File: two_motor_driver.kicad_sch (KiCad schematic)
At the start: 24 parts, among them J1 Conn_01x02, J2 Conn_01x02, J3 Conn_01x08, M1 Conn_01x03, M2 Conn_01x03, SW1 SW_SPDT, SW2 SW_Push, U5 my_buck_boost

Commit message: pcb layout
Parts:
- removed M1, M2, TP2: Conn_01x03, Connector_PinHeader_2.54mm:PinHeader_1x03_P2.54mm_Vertical, symbol Connector_Generic:Conn_01x03
- added FOC1, FOC2: Conn_01x05, Connector_PinSocket_2.54mm:PinSocket_1x05_P2.54mm_Vertical, symbol Connector_Generic:Conn_01x05
- added POT1, RC1, RC2, RC3, SEL1, SEL2: Conn_01x03, Connector_PinHeader_2.54mm:PinHeader_1x03_P2.54mm_Vertical, symbol Connector_Generic:Conn_01x03
- J3: footprint (none) -> Connector_PinSocket_2.54mm:PinSocket_1x08_P2.54mm_Vertical
- renumbered C16 to C1, C15 to C2, D4 to D1, J2 to SEL3
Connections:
- net +3.3V: now also POT1.1 (Pin_1); no longer U5.7 (Reg_out), U5.8 (Reg_out)
- net FOC1_EN: now also FOC1.1 (Pin_1)
- net FOC1_PWM_A: now also FOC1.4 (Pin_4)
- net FOC1_PWM_B: now also FOC1.3 (Pin_3)
- net FOC1_PWM_C: now also FOC1.2 (Pin_2)
- net FOC2_EN: now also FOC2.1 (Pin_1)
- net FOC2_PWM_A: now also FOC2.4 (Pin_4)
- net FOC2_PWM_B: now also FOC2.3 (Pin_3)
- net FOC2_PWM_C: now also FOC2.2 (Pin_2)
- net GND: now also FOC1.5 (Pin_5), FOC2.5 (Pin_5), POT1.3 (Pin_3), RC1.3 (Pin_3), RC2.3 (Pin_3), RC3.3 (Pin_3)
- net MPU6050_SDA: now also SEL2.3 (Pin_3); no longer A1.23 (SDA/A4)
- net RC_Mode: now also RC3.1 (Pin_1)
- net RC_Throttle: now also RC1.1 (Pin_1)
- net +5V: now reaches A1.27 (VUSB/5V)
- net +5V: now also U5.7 (Reg_out), U5.8 (Reg_out), RC1.2 (Pin_2), RC2.2 (Pin_2), RC3.2 (Pin_2)
- net Vcc_Sense: no longer names the net of 10k_2.1, 90k_2.2, D1.3
- net Vcc_Sense: now also SEL1.3 (Pin_3); no longer A1.26 (A7)
- new net A4_in: A1.23 (SDA/A4), SEL2.2 (Pin_2)
- new net A7_in: A1.26 (A7), SEL1.2 (Pin_2)
- new net POT: POT1.2 (Pin_2), SEL2.1 (Pin_1)
- new net RC_Steering: RC2.1 (Pin_1), SEL1.1 (Pin_1)
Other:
- note added: "Pin Signal ---|--------- D1 | TP_ESP32 D2 | FOC1_EN D3 | FOC1_PWM_A D4 | FOC1_PWM_B D5 | FOC1_PWM_C D6 | FOC2_EN D7 | FOC2_PWM_A D8 | FOC2_PWM_B D9 | FOC2_PWM_C D10| ENC1_A D11| ENC1_B D12| ENC2_A D13| On board LED A2 | ENC2_B A4 | MPU6050_SDA / POT A5 | MPU6050_SCL A0 | RC_Throttle A1 | RC_Mode A3 | Hall_1 A6 | Hall_2 A7 | RC_Steering / Vcc IN"
- note added: "Select RC or Vcc in"
- note added: "Select potentiometer or MPU6050_SDA"
- note removed: "Pin Signal ---|--------- D1 | TP_ESP32 D2 | FOC1_EN D3 | FOC1_PWM_A D4 | FOC1_PWM_B D5 | FOC1_PWM_C D6 | FOC2_EN D7 | FOC2_PWM_A D8 | FOC2_PWM_B D9 | FOC2_PWM_C D10| ENC1_A D11| ENC1_B D12| ENC2_A D13| On board LED A2 | ENC2_B A4 | MPU6050_SDA A5 | MPU6050_SCL A0 | RC_Throttle A1 | RC_Mode A3 | Hall_1 A6 | Hall_2 A7 | Vcc_Sense"
- moved on the sheet: 10k_2, 4.7nF_1, 4.7nF_2, 90k_2, A1, C1, C2, D1, J3, R1, R2, TP1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

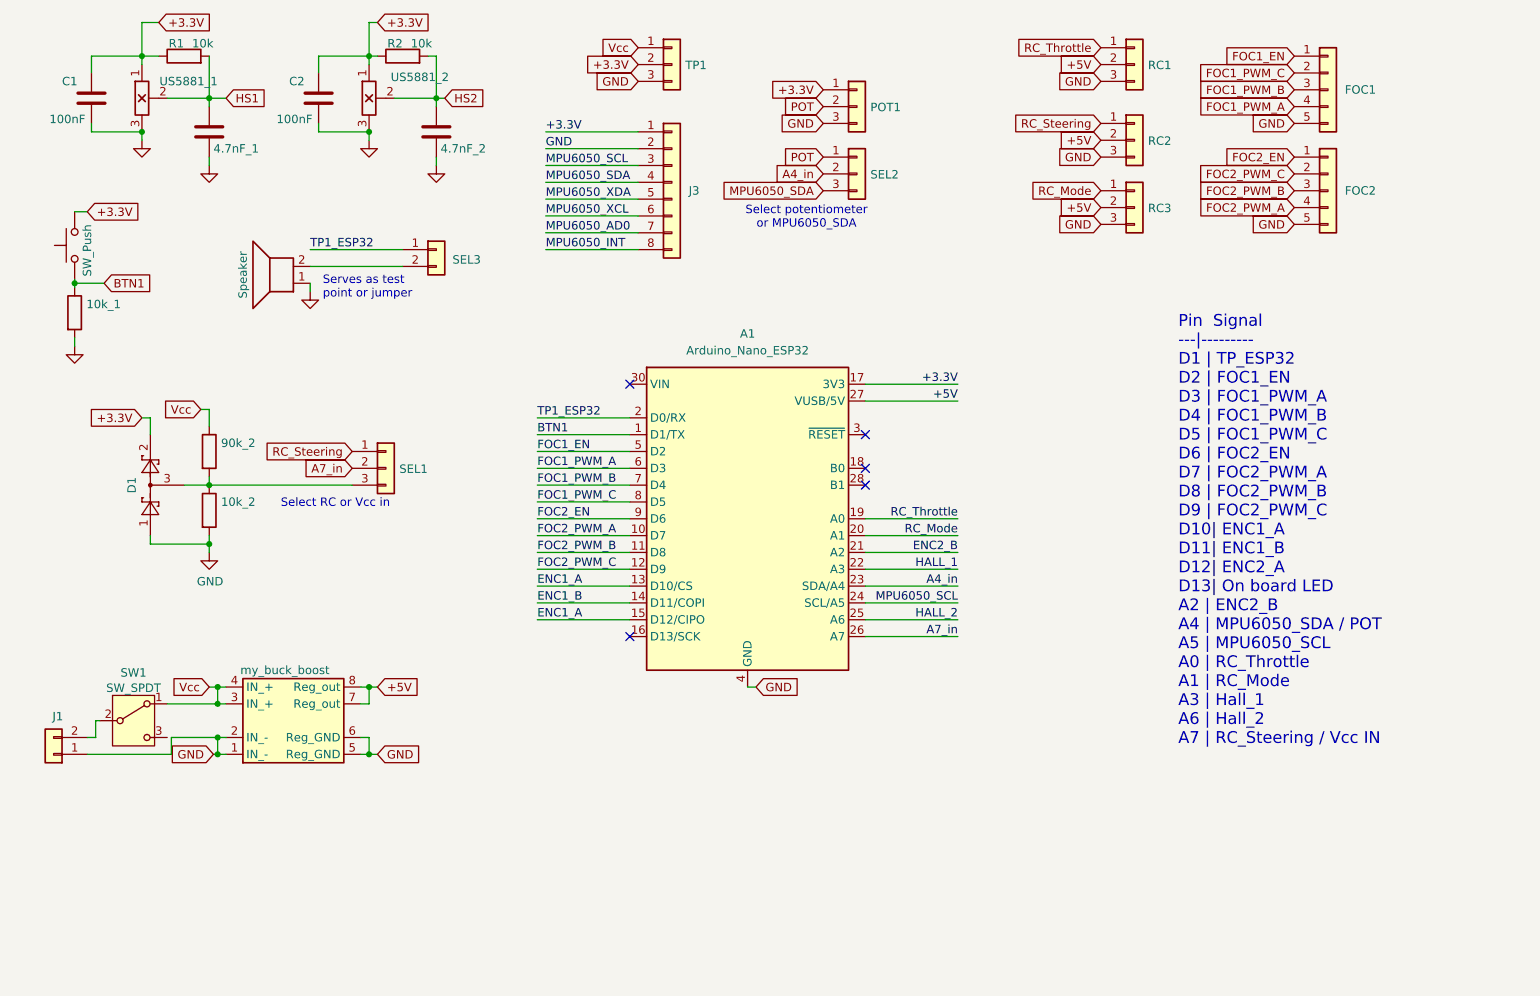
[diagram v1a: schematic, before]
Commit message: converted to teensy 4.0
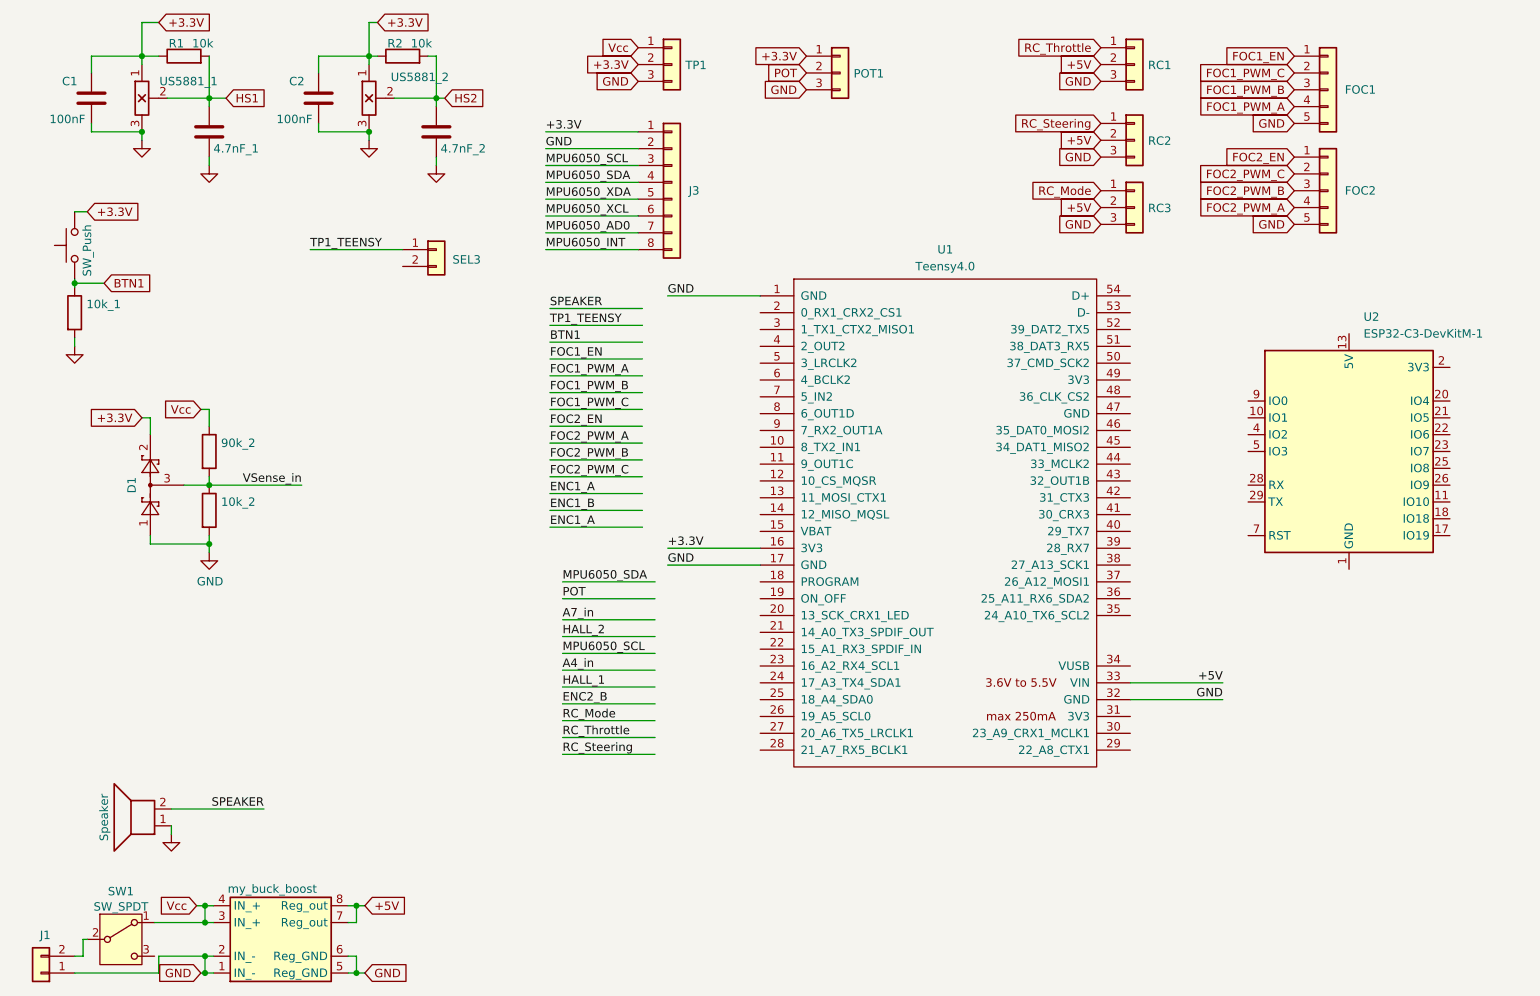
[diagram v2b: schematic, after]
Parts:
- removed A1: Arduino_Nano_ESP32, Module:Arduino_Nano, symbol MCU_Module:Arduino_Nano_ESP32
- removed SEL1, SEL2: Conn_01x03, Connector_PinHeader_2.54mm:PinHeader_1x03_P2.54mm_Vertical, symbol Connector_Generic:Conn_01x03
- added U1: Teensy4.0, simpleFOC_board:Teensy40, symbol teensy:Teensy4.0
- added U2: ESP32-C3-DevKitM-1, RF_Module:ESP32-C3-DevKitM-1, symbol RF_Module:ESP32-C3-DevKitM-1
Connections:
- net +3.3V: now also U1.16 (3V3)
- net +5V: now also U1.33 (VIN)
- net GND: now also U1.1 (GND), U1.17 (GND), U1.32 (GND)
- net VSense_in: now reaches 10k_2.1, 90k_2.2, D1.3
- net at SEL3.2 (Pin_2): no longer LS1.2
- net TP1_ESP32 renamed TP1_TEENSY
- new net: U2.1 (GND), U2.12 (GND), U2.15 (GND), U2.16 (GND), U2.19 (GND), U2.24 (GND), U2.27 (GND), U2.30 (GND), U2.6 (GND), U2.8 (GND)
- new net: U2.13 (5V), U2.14 (5V)
- new net: U2.2 (3V3), U2.3 (3V3)
- new net SPEAKER: LS1.2
- no-connect marks 5 -> 0
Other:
- note removed: "Pin Signal ---|--------- D1 | TP_ESP32 D2 | FOC1_EN D3 | FOC1_PWM_A D4 | FOC1_PWM_B D5 | FOC1_PWM_C D6 | FOC2_EN D7 | FOC2_PWM_A D8 | FOC2_PWM_B D9 | FOC2_PWM_C D10| ENC1_A D11| ENC1_B D12| ENC2_A D13| On board LED A2 | ENC2_B A4 | MPU6050_SDA / POT A5 | MPU6050_SCL A0 | RC_Throttle A1 | RC_Mode A3 | Hall_1 A6 | Hall_2 A7 | RC_Steering / Vcc IN"
- note removed: "Select RC or Vcc in"
- note removed: "Select potentiometer or MPU6050_SDA"
- note removed: "Serves as test point or jumper"
- moved on the sheet: J1, POT1, SW1

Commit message: started layout
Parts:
- removed POT1, TP1: Conn_01x03, Connector_PinHeader_2.54mm:PinHeader_1x03_P2.54mm_Vertical, symbol Connector_Generic:Conn_01x03
- removed SEL3: Conn_01x02, Connector_PinHeader_2.54mm:PinHeader_1x02_P2.54mm_Vertical, symbol Connector_Generic:Conn_01x02
- added ENC1, ENC2: J1, Connector_PinSocket_2.54mm:PinSocket_1x04_P2.54mm_Vertical, symbol Connector_Generic:Conn_01x04
- added J2: ESP PROG, Connector_PinSocket_2.54mm:PinSocket_1x04_P2.54mm_Vertical, symbol Connector_Generic:Conn_01x04
- added J5, J6, J7: Conn_01x01, Connector_PinSocket_2.54mm:PinSocket_1x01_P2.54mm_Vertical, symbol Connector_Generic:Conn_01x01
- added M1, M2: Conn_01x02, Connector_PinHeader_2.54mm:PinHeader_1x02_P2.54mm_Vertical, symbol Connector_Generic:Conn_01x02
- LS1: footprint (none) -> CDS-13138-SMT-TR:SPKR_CDS-13138-SMT-TR
- SW2: footprint (none) -> Button_Switch_SMD:SW_Push_SPST_NO_Alps_SKRK
- renumbered 10k_2 to 10k_1, 10k_1 to 10k_2, R1 to 10k_3, R2 to 10k_4, 90k_2 to 90k_1
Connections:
- net HS1 is gone; now on net HALL_1: 10k_3.2, 4.7nF_1.1, US5881_1.2 (out)
- net HS2 is gone; now on net HALL_2: 10k_4.2, 4.7nF_2.1, US5881_2.2 (out)
- net +3.3V: now also U2.2 (3V3), U2.3 (3V3), ENC1.1 (Pin_1), ENC2.1 (Pin_1), J2.1 (Pin_1), J6.1 (Pin_1)
- net +5V: now also J5.1 (Pin_1)
- net BTN1: now also U1.29 (22_A8_CTX1)
- net ENC1_A: now also U1.2 (0_RX1_CRX2_CS1), ENC1.2 (Pin_2)
- net ENC1_B: now also U1.3 (1_TX1_CTX2_MISO1), ENC1.3 (Pin_3)
- net ENC2_B: now also U1.22 (15_A1_RX3_SPDIF_IN), ENC2.3 (Pin_3)
- net FOC1_EN: now also U1.4 (2_OUT2)
- net FOC1_PWM_A: now also U1.7 (5_IN2)
- net FOC1_PWM_B: now also U1.6 (4_BCLK2)
- net FOC1_PWM_C: now also U1.5 (3_LRCLK2)
- net FOC2_EN: now also U1.8 (6_OUT1D)
- net FOC2_PWM_A: now also U1.11 (9_OUT1C)
- net FOC2_PWM_B: now also U1.10 (8_TX2_IN1)
- net FOC2_PWM_C: now also U1.9 (7_RX2_OUT1A)
- net GND: now also LS1.2, U2.1 (GND), U2.12 (GND), U2.15 (GND), U2.16 (GND), U2.19 (GND), U2.24 (GND), U2.27 (GND), U2.30 (GND), U2.6 (GND), U2.8 (GND), ENC1.4 (Pin_4), ENC2.4 (Pin_4), J2.4 (Pin_4), J7.1 (Pin_1), M1.2 (Pin_2), M2.2 (Pin_2); no longer LS1.1
- net HALL_1: now also U2.21 (IO5)
- net HALL_2: now also U2.20 (IO4)
- net MPU6050_SCL: now also U1.26 (19_A5_SCL0)
- net MPU6050_SDA: now also U1.25 (18_A4_SDA0)
- net RC_Mode: now also U1.24 (17_A3_TX4_SDA1)
- net RC_Steering: now also U1.28 (21_A7_RX5_BCLK1)
- net RC_Throttle: now also U1.27 (20_A6_TX5_LRCLK1)
- net SPEAKER: now also LS1.1, U1.30 (23_A9_CRX1_MCLK1); no longer LS1.2
- net VSense_in: now also U1.21 (14_A0_TX3_SPDIF_OUT)
- net Vcc: now also M1.1 (Pin_1), M2.1 (Pin_1)
- net ESP32_CS: now reaches U2.11 (IO10)
- net ESP32_CS: now also U1.12 (10_CS_MQSR)
- net ESP32_CLK: now reaches U2.22 (IO6)
- net ESP32_CLK: now also U1.20 (13_SCK_CRX1_LED)
- net ESP32_MOSI: now reaches U2.23 (IO7)
- net ESP32_MOSI: now also U1.13 (11_MOSI_CTX1)
- net ESP32_RX: now reaches U2.28 (RX)
- net ESP32_RX: now also J2.2 (Pin_2)
- net ESP32_TX: now reaches U2.29 (TX)
- net ESP32_TX: now also J2.3 (Pin_3)
- net ESP32_MISO: now reaches U2.4 (IO2)
- net ESP32_MISO: now also U1.14 (12_MISO_MQSL)
- net ENC2_A: now reaches U1.23 (16_A2_RX4_SCL1)
- net ENC2_A: now also ENC2.2 (Pin_2)
- no-connect marks 0 -> 14
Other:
- moved on the sheet: 10k_1, 90k_1, D1, J3, U1

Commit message: completing traces
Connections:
- net +3.3V: no longer U2.2 (3V3), U2.3 (3V3)
- net +5V: now also U2.13 (5V), U2.14 (5V)
- new net: U2.2 (3V3), U2.3 (3V3)
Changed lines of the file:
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@@
-	)
-	(no_connect
-		(at 209.55 55.88)
 	)
 	(no_connect
@@
 	)
 	(no_connect
+		(at 224.79 60.96)
+	)
+	(no_connect
 		(at 194.31 86.36)
 	)
@@
 	(wire
 		(pts
+			(xy 209.55 53.34) (xy 209.55 55.88)
+		)
+		(stroke
+			(width 0)
+			(type default)
+		)
+	)
+	(wire
+		(pts
 			(xy 21.59 57.15) (xy 26.035 57.15)
 		)
@@
 	(wire
 		(pts
+			(xy 210.82 53.34) (xy 209.55 53.34)
+		)
+		(stroke
+			(width 0)
+			(type default)
+		)
+	)
+	(wire
+		(pts
 			(xy 64.77 59.69) (xy 50.8 59.69)
 		)
@@
 		(pts
 			(xy 88.9 64.77) (xy 102.87 64.77)
-		)
-		(stroke
-			(width 0)
-			(type default)
-		)
-	)
-	(wire
-		(pts
-			(xy 238.76 60.96) (xy 224.79 60.96)
 		)
 		(stroke
@@
 			)
 			(justify left bottom)
-		)
-	)
-	(label "+3.3V"
-		(at 238.76 60.96 180)
-		(effects
-			(font
-				(size 1.27 1.27)
-			)
-			(justify right bottom)
 		)
 	)
@@
 				(hide yes)
 			)
+		)
+	)
+	(global_label "+5V"
+		(shape input)
+		(at 210.82 53.34 0)
+		(fields_autoplaced yes)
+		(effects
+			(font
+				(size 1.27 1.27)
+			)
+			(justify left)
+		)
+		(property "Intersheetrefs" "${INTERSHEET_REFS}"
+			(at 217.0215 53.34 0)
+			(effects
+				(font
+					(size 1.27 1.27)
+				)
+				(justify left)
+				(hide yes)
+			)
